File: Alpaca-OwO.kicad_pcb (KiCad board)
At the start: 4 copper layers, 96 x 45 mm, 43 parts, among them J1 SWD, J2 PS360 ST1, J3 PS360 ST2, J4 Stick, J5 USB_B, J6 Pwny Pr0t, J7 I2C Quick connect, Q1 CJL3415, SW1 Reset, SW2 I2C Pullup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

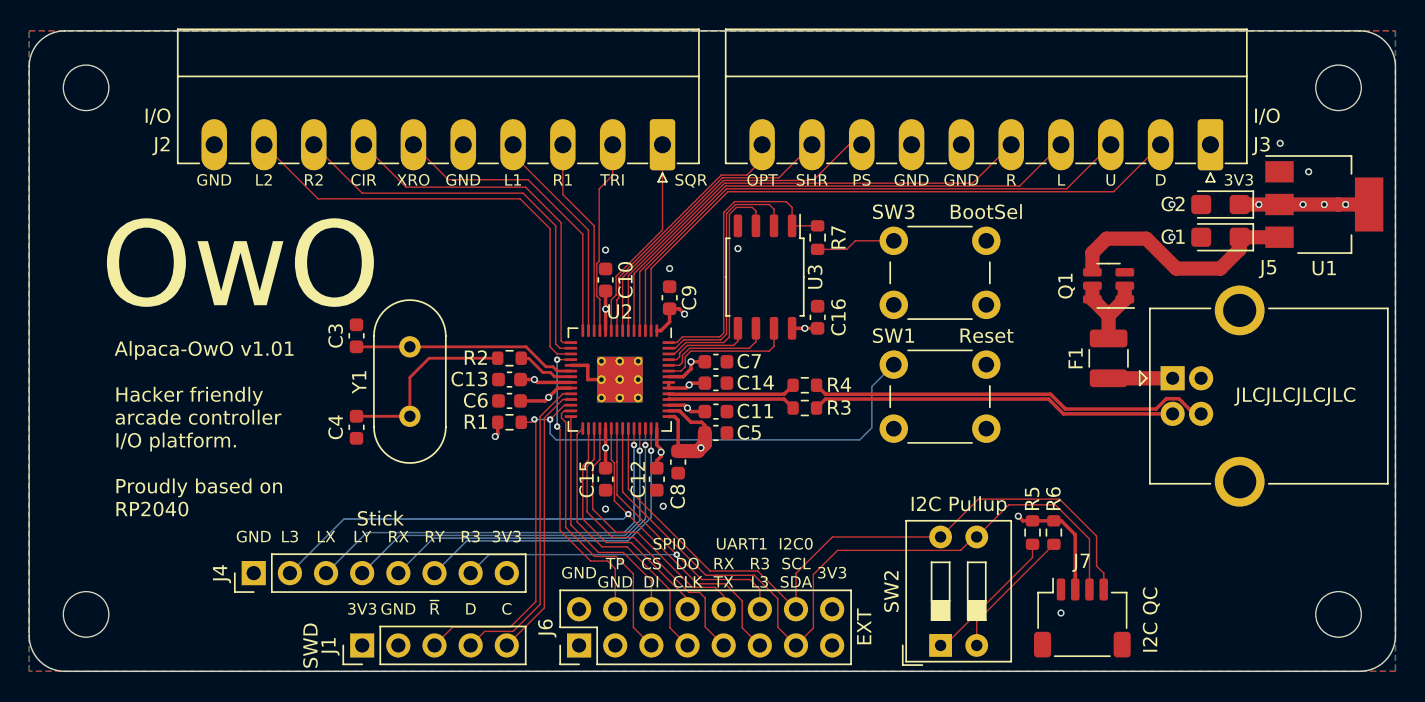
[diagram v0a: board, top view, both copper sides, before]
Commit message: V1.10 PCB
Change the via size to be 0.55/0.3 so the annular ring width stay consistent with JLC's design rule.
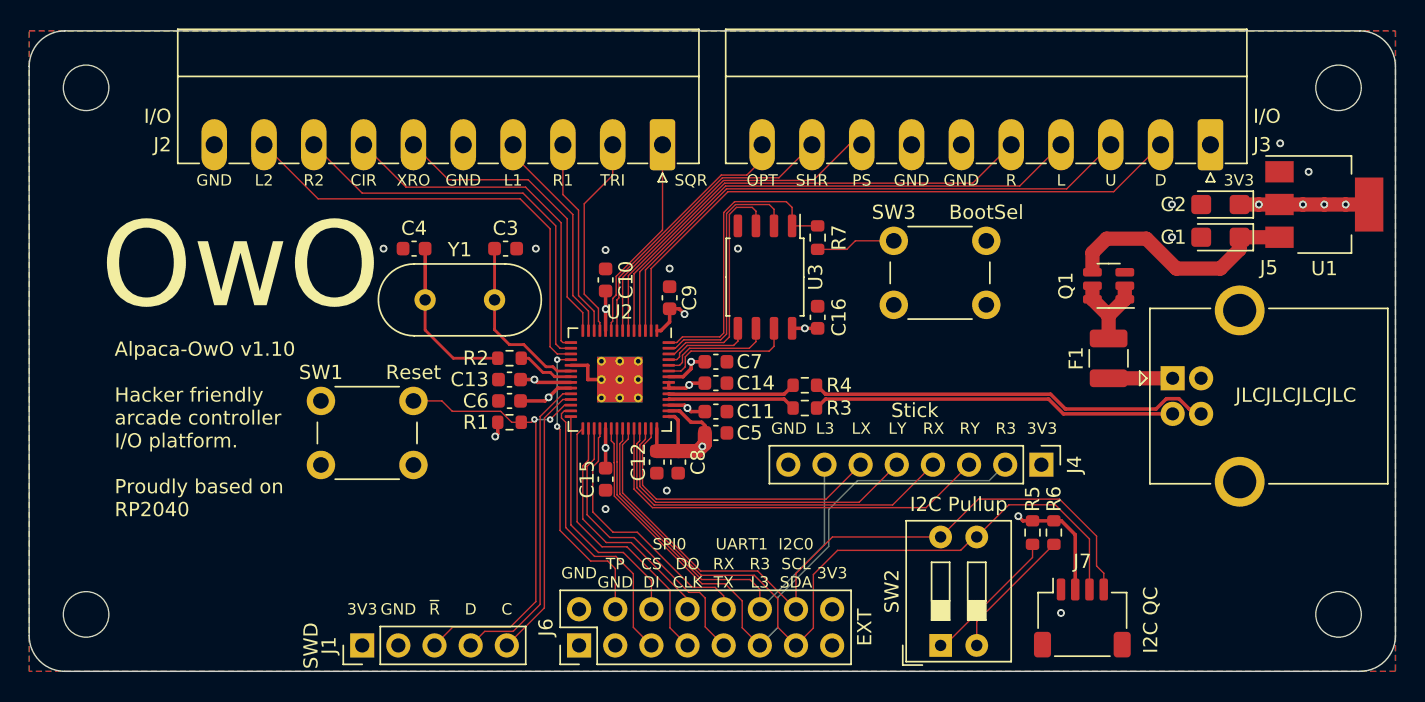
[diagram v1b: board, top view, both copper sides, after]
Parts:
- moved J4 55.9 mm to (178.8, 108.5), turned to -90 degrees
- moved SW1 40.3 mm to (128.2, 104.0)
- moved C4 13.2 mm to (134.7, 93.3), turned to 0 degrees
- moved C3 12.1 mm to (141.2, 93.3), turned to 0 degrees
- moved Y1 8.25 mm to (135.5, 97.0), turned to 0 degrees
- moved C12 1.20 mm to (151.8, 108.3)
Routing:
- net /~{RESET}: track 54.4 -> 33.4 mm
- net Net-(C3-Pad1): track 15.8 -> 12.3 mm
- net /KEY_R3: track 33.9 -> 30.9 mm, vias 1 -> 0
- net Net-(C4-Pad2): track 13.2 -> 15.4 mm
- net /STK_RY: track 23.1 -> 21.0 mm, vias 1 -> 0
- net /STK_RX: track 25.3 -> 23.8 mm, vias 1 -> 0
- net /STK_LY: track 27.5 -> 26.7 mm, vias 1 -> 0
- net /KEY_TRI: track 13.6 -> 14.3 mm
- net /I2C0_SCL: track 50.4 -> 51.1 mm
- net /KEY_L3: track 46.2 -> 45.8 mm, vias 1 -> 0
- net /STK_LX: track 29.7 -> 29.6 mm, vias 1 -> 0
- net +3V3: track 48.2 -> 48.3 mm, vias 14 -> 13
- net GND: vias 10 -> 12
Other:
- board text added: "Alpaca-OwO v1.10 Hacker friendly arcade controller I/O platform. Proudly based on RP2040"
- board text removed: "Alpaca-OwO v1.01 Hacker friendly arcade controller I/O platform. Proudly based on RP2040"
- board text removed: "The ADC traces are currently routed on the back of the board on top of power plane. This is less than ideal but should be OK if they are only used for low freq low res ADC sampling (e.g. as analog sticks). Resolving this would require shifting a large amount of components or even redo the whole board so might not be worth it for now."
